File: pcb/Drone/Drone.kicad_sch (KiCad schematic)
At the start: 66 parts, among them J1 USB_C_Receptacle_USB2.0_16P, J10 JST1.25, J2 JST1.25, J3 JST1.25, J4 JST1.25, J5 JST1.25, J6 JST1.25, J7 JST1.25, J8 JST1.25, J9 JST1.25, Q1 SS8050, Q2 SS8050, Q3 Si2301, SW1 RST, SW2 BOOT, U1 esp32s3_wroom1, U10 AP2112K-3.3, U2 DW01A, U3 Ra02, U4 USBLC6-2SC6, U5 8205, U6 CP2102, U8 GY-87, U9 ME6211C33M5

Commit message: pcb layout: complete component positions
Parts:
- removed D5: D, symbol Device:D_Schottky
- removed J10: JST1.25, Drone:JST_1.25mm_RA_SMD_4P, symbol Connector:Conn_01x04_Socket
- removed J2, J3, J4, J6: JST1.25, Drone:JST_1.25mm_RA_SMD_3P, symbol Connector:Conn_01x03_Pin
- removed U3: Ra02, Drone:RA-01H, symbol RF:Ra02
- removed U7: (no value), symbol custom_symbols:MicroSD
- added C13: 22u, Capacitor_SMD:C_0805_2012Metric, symbol Device:C_Small
- added C14, C3, C5: 0.1u, Capacitor_SMD:C_0805_2012Metric, symbol Device:C_Small
- added C19: 0.1u, Capacitor_SMD:C_0402_1005Metric, symbol Device:C
- added C4: 10u, Capacitor_SMD:C_0805_2012Metric, symbol Device:C_Small
- added D3: 1N5819, Diode_SMD:D_SOD-123, symbol Device:D_Schottky
- added J10, J11, J9: 2.54mm, Connector_PinSocket_2.54mm:PinSocket_1x07_P2.54mm_Vertical, symbol Connector:Conn_01x07_Socket
- added J14: Micro_SD_Card_Det1, Drone_local_footprints:Micro_SD_Card_Socket, symbol Connector:Micro_SD_Card_Det1
- added J15: JST1.25, Connector_PinHeader_2.54mm:PinHeader_1x07_P2.54mm_Vertical, symbol Connector:Conn_01x07_Socket
- added J2, J3, J4, J5: JST1.25, Drone_local_footprints:JST_1.25mm_RA_SMD_3P, symbol Connector:Conn_01x03_Socket
- added R10, R9: 10K, Resistor_SMD:R_0402_1005Metric, symbol Device:R_Small_US
- added R12, R16, R18, R19: 22R, Resistor_SMD:R_0402_1005Metric, symbol Device:R_Small_US
- added R25, R26: 0R, Resistor_SMD:R_0402_1005Metric, symbol Device:R_Small_US
- added RN1: 10K, Resistor_SMD:R_Array_Concave_4x0603, symbol Device:R_Pack04
- added SW2: USER, Button_Switch_SMD:SW_SPST_EVQP2_MiddlePushTravel_H2.5mm, symbol Switch:SW_Push
- added U8: Ai-Thinker-Ra-02, RF_Module:Ai-Thinker-Ra-01-LoRa, symbol RF_Module:Ai-Thinker-Ra-02
- D2: renamed from D4; value D -> 1N5819; footprint (none) -> Diode_SMD:D_SOD-123; Supplier (none) -> https://icdayroi.com/diode-1n5819-sod123-size-1206
- J12: renamed from J9; footprint Drone:JST_1.25mm_RA_SMD_4P -> Drone_local_footprints:JST_1.25mm_RA_SMD_4P
- J13: renamed from J5; footprint Drone:JST_1.25mm_RA_SMD_2P -> Drone_local_footprints:JST_1.25mm_RA_SMD_2P
- J6: renamed from J7; footprint Drone:JST_1.25mm_RA_SMD_4P -> Drone_local_footprints:JST_1.25mm_RA_SMD_4P
- J8: footprint Drone:JST_1.25mm_RA_SMD_8P -> Drone_local_footprints:JST_1.25mm_RA_SMD_8P
- R20: renamed from R15; footprint (none) -> Resistor_SMD:R_0402_1005Metric
- R21: renamed from R16; footprint (none) -> Resistor_SMD:R_0402_1005Metric
- R22: renamed from R17; footprint (none) -> Resistor_SMD:R_0402_1005Metric
- R23: renamed from R18; footprint (none) -> Resistor_SMD:R_0402_1005Metric
- R5: renamed from R4; Supplier (none) -> https://chipn24.com/50-con-dien-tro-dan-smd-0402-22k-1-id10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
- R6: renamed from R11; Supplier (none) -> https://chipn24.com/50-con-dien-tro-dan-smd-0402-47k-1-id10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
- U3: renamed from U8; footprint Drone:GY-87 -> Drone_local_footprints:GY-87
- U6: renamed from U10; Supplier (none) -> https://shopee.vn/Set-10-Linh-Ki%E1%BB%87n-%C4%90i%E1%BB%87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
- renumbered C11 to C1, C19 to C10, C21 to C11, C20 to C12, C5 to C16, C7 to C17, C1 to C18, C12 to C2, C14 to C20, C2 to C21, C13 to C6, C16 to C7, C18 to C8, C17 to C9, D3 to D1, D1 to D4, D2 to D5, H3 to H2, H2 to H3, R6 to R1, R14 to R11, R12 to R13, R8 to R14, R13 to R15, R3 to R17, R7 to R2, R5 to R3, R10 to R4, R1 to R7, R2 to R8, SW2 to SW1, SW1 to SW3, U4 to U1, U6 to U2, U2 to U4, U9 to U7, U1 to U9
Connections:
- net MISO is gone; now on net GPIO13: J8.4 (Pin_4)
- net +3V3: now also C13.2, C14.1, C4.1, C5.1, J14.4 (VDD), J15.1 (Pin_1), R10.1, R9.1, RN1.5 (R4.2), RN1.6 (R3.2), RN1.7 (R2.2), RN1.8 (R1.2), U8.3 (VDD)
- net +3V3_SENS: now also U3.2 (3.3V), C3.1
- net GND: now also U3.3 (GND), C13.1, C14.2, C19.2, C3.2, C4.2, C5.2, J14.6 (VSS), J14.SH (SHIELD), J15.2 (Pin_2), J2.1 (Pin_1), J3.1 (Pin_1), J4.1 (Pin_1), J5.1 (Pin_1), J9.7 (Pin_7), SW2.1, U8.1 (GND), U8.16 (GND), U8.2 (GND), U8.9 (GND)
- net GPIO11: now also R18.1
- net GPIO12: now also R19.1
- net GPIO13: now also R12.1, R16.1, RN1.3 (R3.1)
- net MOSI: now also J14.3 (CMD), R18.2, RN1.4 (R4.1), U8.14 (MOSI)
- net PWM1: now also J2.3 (Pin_3)
- net PWM2: now also J11.6 (Pin_6), J3.3 (Pin_3)
- net PWM3: now also J11.5 (Pin_5), J4.3 (Pin_3)
- net PWM4: now also J11.4 (Pin_4), J5.3 (Pin_3)
- net SCK: now also J14.5 (CLK), R19.2, U8.12 (SCK)
- net SCL0: now also U3.4 (SCL), J15.3 (Pin_3)
- net SDA0: now also U3.5 (SDA), J15.4 (Pin_4)
- net VBEC: now also D3.2 (A), J2.2 (Pin_2)
- net DRDY: now reaches U3.8 (DRDY)
- net GPIO35: no longer names the net of U9.28 (IO35)
- net GPIO36: no longer names the net of U9.29 (IO36)
- net GPIO37: no longer names the net of U9.30 (IO37)
- net GPIO45: no longer names the net of U9.26 (IO45)
- net GPIO46: no longer names the net of U9.16 (IO46)
- net RGB_POW renamed +5V
- net +5V: now also D3.1 (K), J10.7 (Pin_7)
- net RXD: no longer names the net of U2.25 (RXD)
- net RXD: now also R25.1
- net TXD: no longer names the net of U2.26 (TXD)
- net TXD: now also R26.1
- net U0RXD renamed RXD0
- net RXD0: now also R26.2
- net U0TXD renamed TXD0
- net TXD0: now also R25.2
- new net: R16.2, U8.13 (MISO)
- new net: J14.1 (DAT2), R9.2
- new net: J14.7 (DAT0), R12.2
- new net: J14.8 (DAT1), RN1.2 (R2.1)
- new net CARD_DETECT: J14.9 (DET), RN1.1 (R1.1)
- new net CS_RF: U8.15 (~{NSS})
- new net CS_uSD: J14.2 (DAT3/CD), R10.2
- new net PPM/PWM1: J11.7 (Pin_7)
- new net PWM5: J11.3 (Pin_3)
- new net PWM6: J11.2 (Pin_2)
- new net RF_RST: U8.4 (~{RESET})
- new net USR_BUTTON: C19.1, SW2.2
- no-connect marks 17 -> 28
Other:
- note added: "Black box"
- note added: "IMU"
- note added: "MS5611"
- note added: "RF Module"
- note added: "RGB Led"
- note added: "RX"
- note removed: "PERIPHERALS"
- note removed: "black box receiver connector telemetry"
- moved on the sheet: C10, C11, C12, C18, C20, C21, C6, C7, C8, C9, D1, D2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

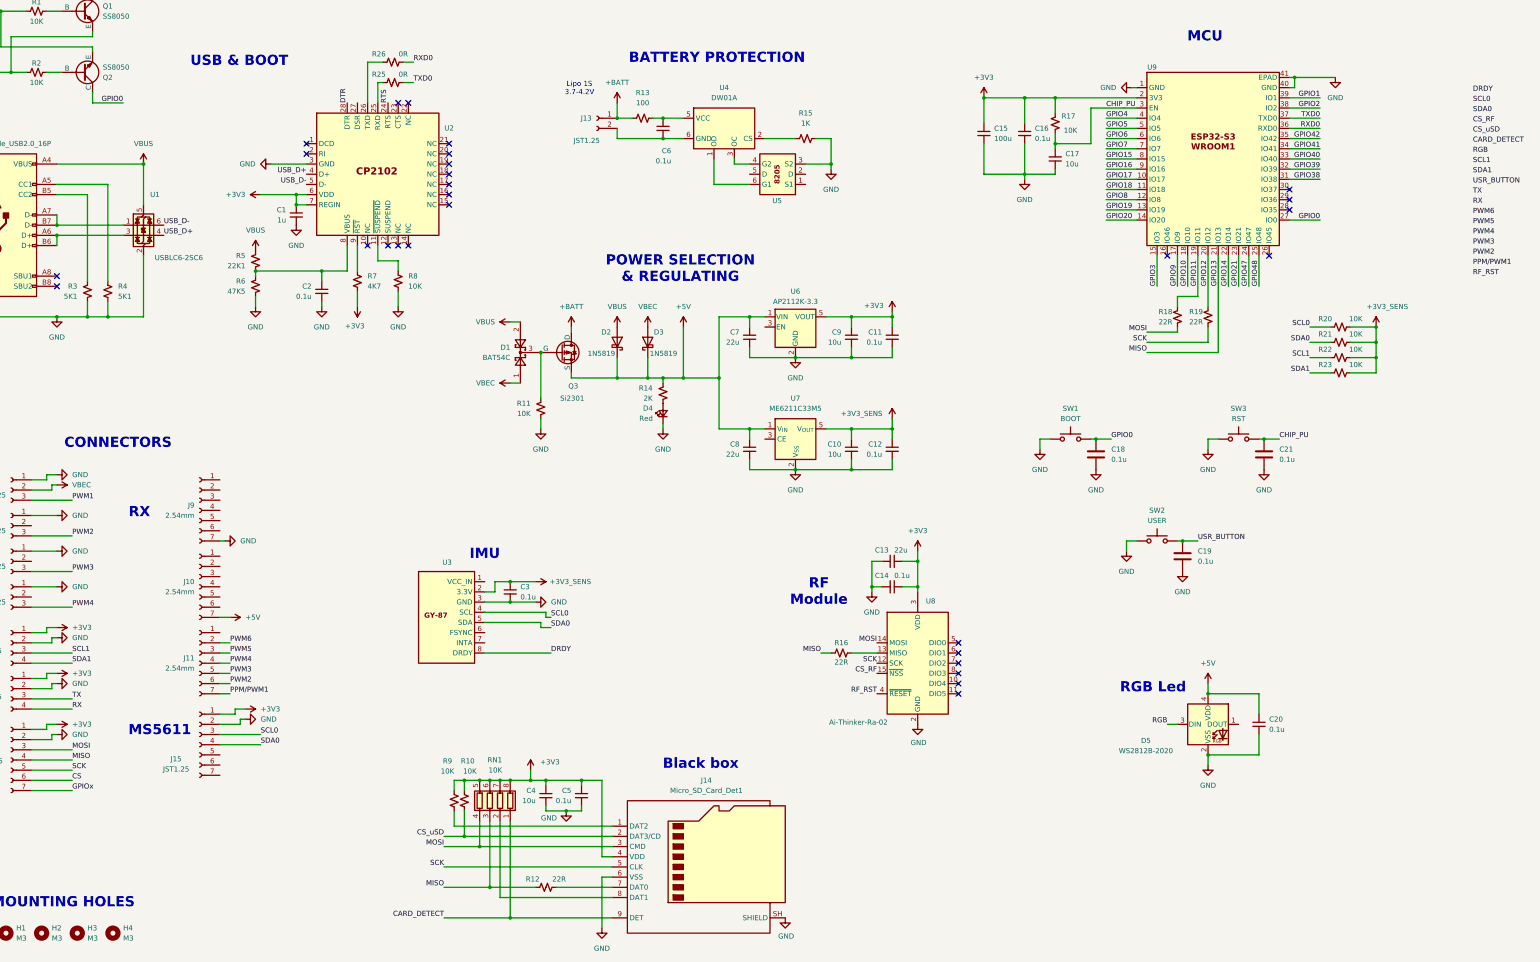
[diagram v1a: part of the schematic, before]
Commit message: fc pcb: done; 3d model: initial frame and physical properties
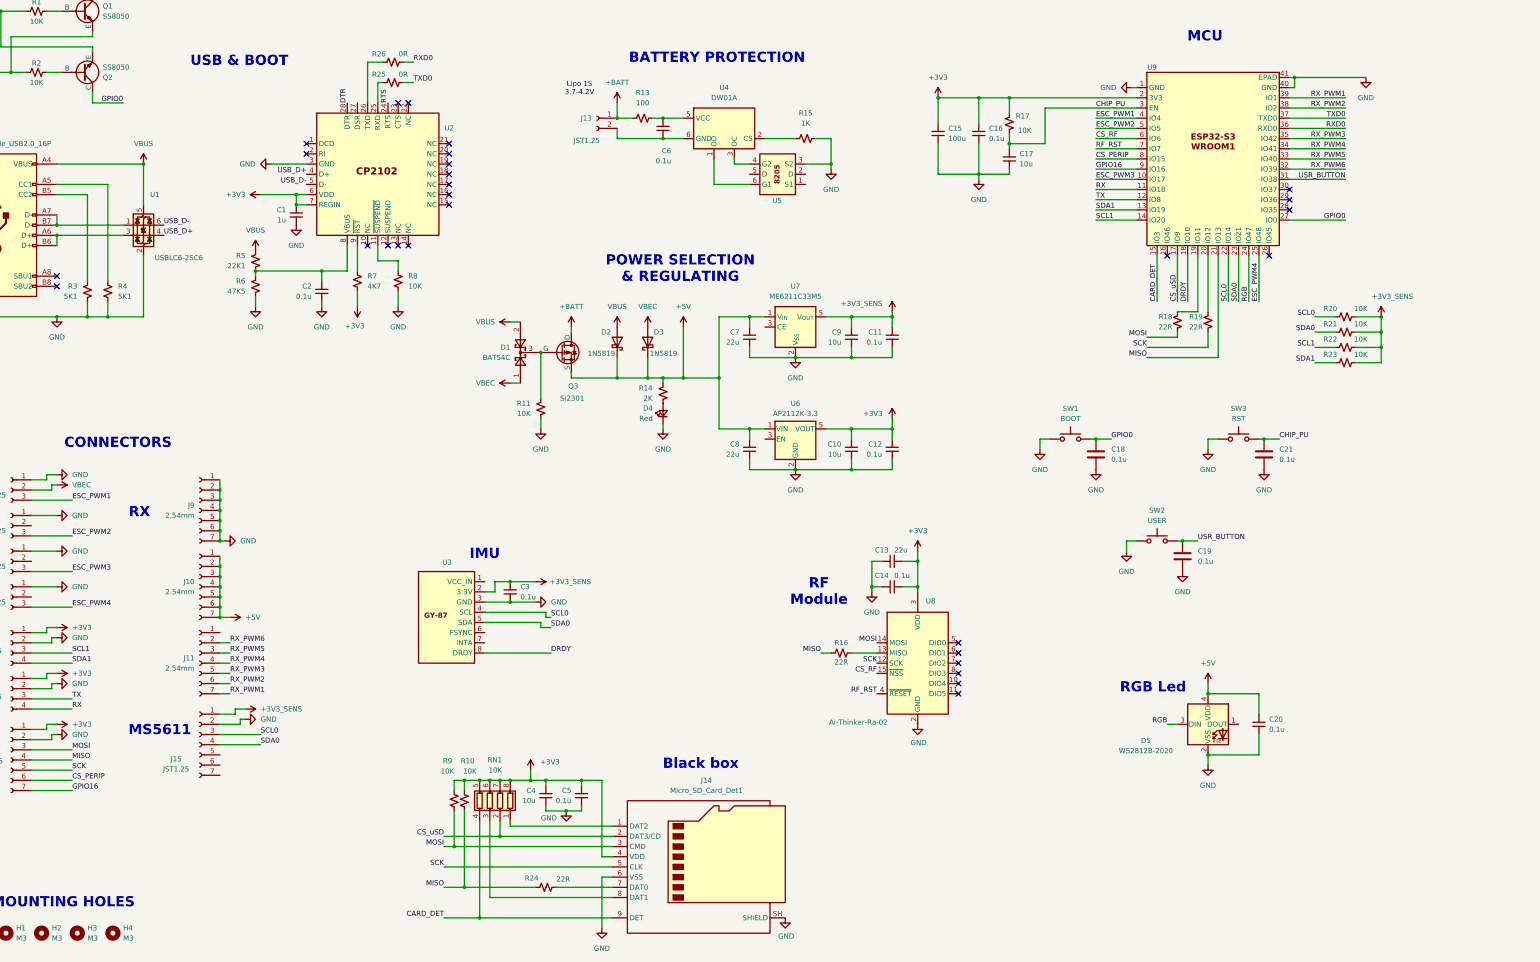
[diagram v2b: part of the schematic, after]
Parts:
- removed R12: 22R, Resistor_SMD:R_0402_1005Metric, symbol Device:R_Small_US
- added R24: 22R, Resistor_SMD:R_0402_1005Metric, symbol Device:R_Small_US
- J12, J6: footprint Drone_local_footprints:JST_1.25mm_RA_SMD_4P -> Local Footprints:JST_1.25mm_RA_SMD_4P
- J13: footprint Drone_local_footprints:JST_1.25mm_RA_SMD_2P -> Local Footprints:JST_1.25mm_RA_SMD_2P
- J14: footprint Drone_local_footprints:Micro_SD_Card_Socket -> Local Footprints:Micro_SD_Card_Socket
- J2, J3, J4, J5: footprint Drone_local_footprints:JST_1.25mm_RA_SMD_3P -> Local Footprints:JST_1.25mm_RA_SMD_3P
- J8: footprint Drone_local_footprints:JST_1.25mm_RA_SMD_8P -> Local Footprints:JST_1.25mm_RA_SMD_8P
- U3: footprint Drone_local_footprints:GY-87 -> Local Footprints:GY-87
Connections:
- net GPIO10 is gone; now on net DRDY: U9.18 (IO10)
- net GPIO14 is gone; now on net SCL0: U9.22 (IO14)
- net GPIO15 is gone; now on net CS_PERIP: U9.8 (IO15)
- net GPIO18 is gone; now on net RX: U9.11 (IO18)
- net GPIO19 is gone; now on net SDA1: U9.13 (IO19)
- net GPIO20 is gone; now on net SCL1: U9.14 (IO20)
- net GPIO21 is gone; now on net SDA0: U9.23 (IO21)
- net GPIO3 is gone; now on net CARD_DET: U9.15 (IO3)
- net GPIO38 is gone; now on net USR_BUTTON: U9.31 (IO38)
- net GPIO47 is gone; now on net RGB: U9.24 (IO47)
- net GPIO6 is gone; now on net CS_RF: U9.6 (IO6)
- net GPIO7 is gone; now on net RF_RST: U9.7 (IO7)
- net GPIO8 is gone; now on net TX: U9.12 (IO8)
- net GPIO9 is gone; now on net CS_uSD: U9.17 (IO9)
- net GPIOx is gone; now on net GPIO16: J8.7 (Pin_7)
- net PPM/PWM1 is gone; now on net RX_PWM1: J11.7 (Pin_7)
- net PWM1 is gone; now on net ESC_PWM1: J2.3 (Pin_3)
- net PWM5 is gone; now on net RX_PWM5: J11.3 (Pin_3)
- net PWM6 is gone; now on net RX_PWM6: J11.2 (Pin_2)
- net +3V3: now also C10.1, C12.1; no longer C11.1, C9.1, J15.1 (Pin_1)
- net +3V3_SENS: now also C11.1, C9.1, J15.1 (Pin_1); no longer C10.1, C12.1
- net +5V: now also J10.1 (Pin_1), J10.2 (Pin_2), J10.3 (Pin_3), J10.4 (Pin_4), J10.5 (Pin_5), J10.6 (Pin_6)
- net CS_uSD: now also RN1.2 (R2.1); no longer R10.2
- net GND: now also J9.1 (Pin_1), J9.2 (Pin_2), J9.3 (Pin_3), J9.4 (Pin_4), J9.5 (Pin_5), J9.6 (Pin_6)
- net MOSI: now also R9.2; no longer RN1.4 (R4.1)
- net at J14.1 (DAT2): now also RN1.1 (R1.1); no longer R9.2
- net at J14.7 (DAT0): now also R24.2
- net at J14.8 (DAT1): now also RN1.3 (R3.1); no longer RN1.2 (R2.1)
- net CARD_DETECT renamed CARD_DET
- net CARD_DET: now also RN1.4 (R4.1); no longer RN1.1 (R1.1)
- net CS renamed CS_PERIP
- net GPIO1 renamed RX_PWM1
- net GPIO11: no longer names the net of R18.1, U9.19 (IO11)
- net GPIO12: no longer names the net of R19.1, U9.20 (IO12)
- net GPIO13 renamed MISO
- net MISO: now also R10.2, R24.1; no longer RN1.3 (R3.1)
- net GPIO17 renamed ESC_PWM3
- net ESC_PWM3: now also J4.3 (Pin_3)
- net GPIO2 renamed RX_PWM2
- net RX_PWM2: now also J11.6 (Pin_6)
- net GPIO39 renamed RX_PWM6
- net GPIO4 renamed ESC_PWM1
- net GPIO40 renamed RX_PWM5
- net GPIO41 renamed RX_PWM4
- net RX_PWM4: now also J11.4 (Pin_4)
- net GPIO42 renamed RX_PWM3
- net RX_PWM3: now also J11.5 (Pin_5)
- net GPIO48 renamed ESC_PWM4
- net ESC_PWM4: now also J5.3 (Pin_3)
- net GPIO5 renamed ESC_PWM2
- net ESC_PWM2: now also J3.3 (Pin_3)
- removed net PWM2: J11.6 (Pin_6), J3.3 (Pin_3)
- removed net PWM3: J11.5 (Pin_5), J4.3 (Pin_3)
- removed net PWM4: J11.4 (Pin_4), J5.3 (Pin_3)
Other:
- title: OISP Drone: Flight Controller -> Modus Project: Flight Controller
- moved on the sheet: C15, C16, C17, R17, R18, R19, R20, R21, R22, R23

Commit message: development: 3d, power board, fc
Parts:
- C11, C12, C14, C3, C5: footprint Capacitor_SMD:C_0805_2012Metric -> Capacitor_SMD:C_0402_1005Metric
- J10, J11, J9: footprint Connector_PinSocket_2.54mm:PinSocket_1x07_P2.54mm_Vertical -> Local Footprints:_PinSocket_1x07_P2.54mm_Vertical
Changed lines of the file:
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@@
 			)
 		)
-		(property "Footprint" "Capacitor_SMD:C_0805_2012Metric"
+		(property "Footprint" "Capacitor_SMD:C_0402_1005Metric"
 			(at 275.59 138.43 0)
 			(hide yes)
@@
 			)
 		)
-		(property "Footprint" "Connector_PinSocket_2.54mm:PinSocket_1x07_P2.54mm_Vertical"
+		(property "Footprint" "Local Footprints:_PinSocket_1x07_P2.54mm_Vertical"
 			(at 102.87 191.77 0)
 			(hide yes)
@@
 			)
 		)
-		(property "Footprint" "Capacitor_SMD:C_0805_2012Metric"
+		(property "Footprint" "Capacitor_SMD:C_0402_1005Metric"
 			(at 198.12 224.79 0)
 			(hide yes)
@@
 			)
 		)
-		(property "Footprint" "Connector_PinSocket_2.54mm:PinSocket_1x07_P2.54mm_Vertical"
+		(property "Footprint" "Local Footprints:_PinSocket_1x07_P2.54mm_Vertical"
 			(at 102.87 172.72 0)
 			(hide yes)
@@
 			)
 		)
-		(property "Footprint" "Connector_PinSocket_2.54mm:PinSocket_1x07_P2.54mm_Vertical"
+		(property "Footprint" "Local Footprints:_PinSocket_1x07_P2.54mm_Vertical"
 			(at 102.87 153.67 0)
 			(hide yes)
@@
 			)
 		)
-		(property "Footprint" "Capacitor_SMD:C_0805_2012Metric"
+		(property "Footprint" "Capacitor_SMD:C_0402_1005Metric"
 			(at 275.59 110.49 0)
 			(hide yes)
@@
 			)
 		)
-		(property "Footprint" "Capacitor_SMD:C_0805_2012Metric"
+		(property "Footprint" "Capacitor_SMD:C_0402_1005Metric"
 			(at 180.34 173.99 0)
 			(hide yes)
@@
 			)
 		)
-		(property "Footprint" "Capacitor_SMD:C_0805_2012Metric"
+		(property "Footprint" "Capacitor_SMD:C_0402_1005Metric"
 			(at 275.59 172.72 0)
 			(hide yes)

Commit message: rtos architecture
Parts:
- C1: value 1u -> 0.1u
- J15: value JST1.25 -> 2.54mm
- R13: value 100 -> 100R
- R14: value 2K -> 330R
- R7: value 4K7 -> 5K1
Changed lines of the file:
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@@
 			)
 		)
-		(property "Value" "1u"
+		(property "Value" "0.1u"
 			(at 124.46 81.2862 0)
 			(show_name no)
@@
 			)
 		)
-		(property "Value" "100"
+		(property "Value" "100R"
 			(at 213.36 52.07 90)
 			(show_name no)
@@
 			)
 		)
-		(property "Value" "JST1.25"
+		(property "Value" "2.54mm"
 			(at 97.028 218.186 0)
 			(show_name no)
@@
 			)
 		)
-		(property "Value" "4K7"
+		(property "Value" "5K1"
 			(at 144.78 97.7899 0)
 			(show_name no)
@@
 			)
 		)
-		(property "Value" "2K"
+		(property "Value" "330R"
 			(at 215.8277 125.7299 0)
 			(show_name no)
